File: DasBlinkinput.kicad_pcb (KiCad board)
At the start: 4 copper layers, 25.4 x 50.8 mm, 34 parts, among them P101 CONN_01X02, P102 CONN_01X01, P103 CONN_01X01, P104 CONN_01X01, P105 CONN_01X05, P201 CONN_01X01, P301 CONN_01X01, P401 CONN_01X01, P501 CONN_01X01, U101 LP2980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

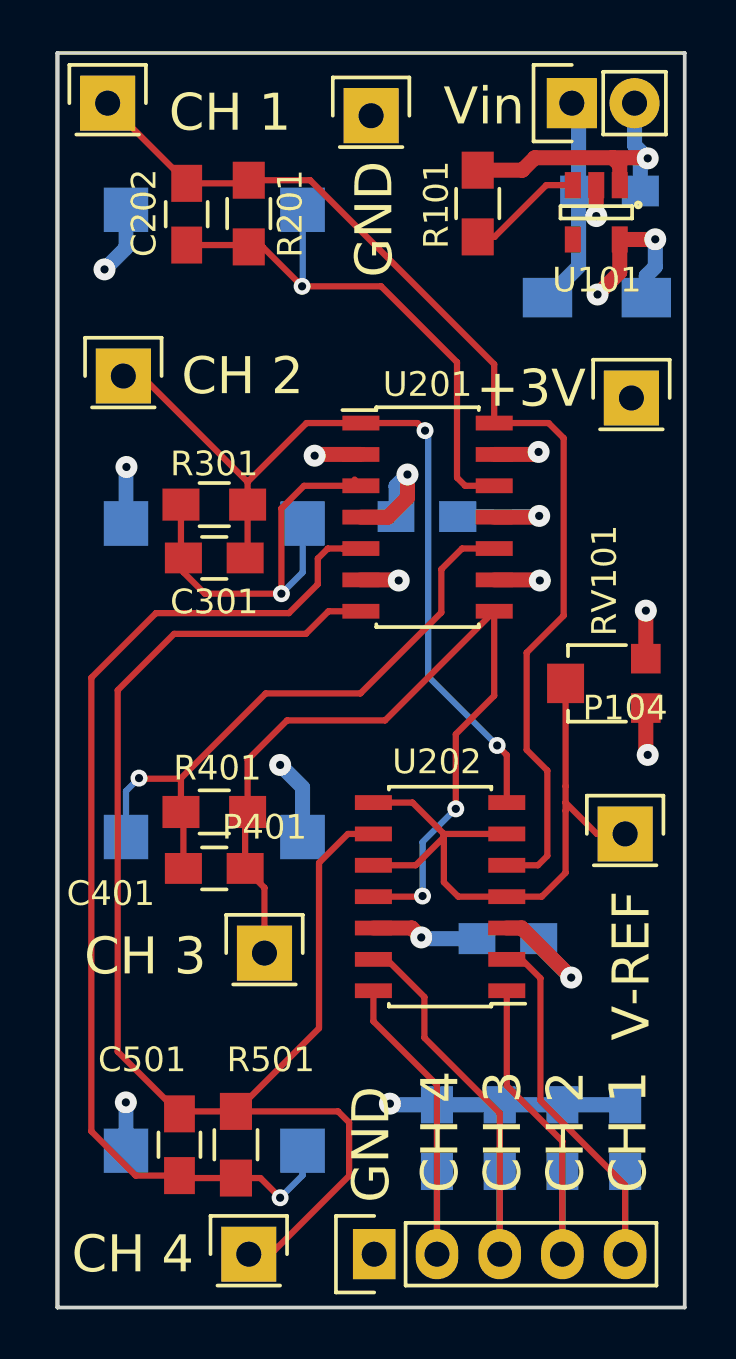
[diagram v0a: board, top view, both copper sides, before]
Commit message: resized labels and added board name and rev
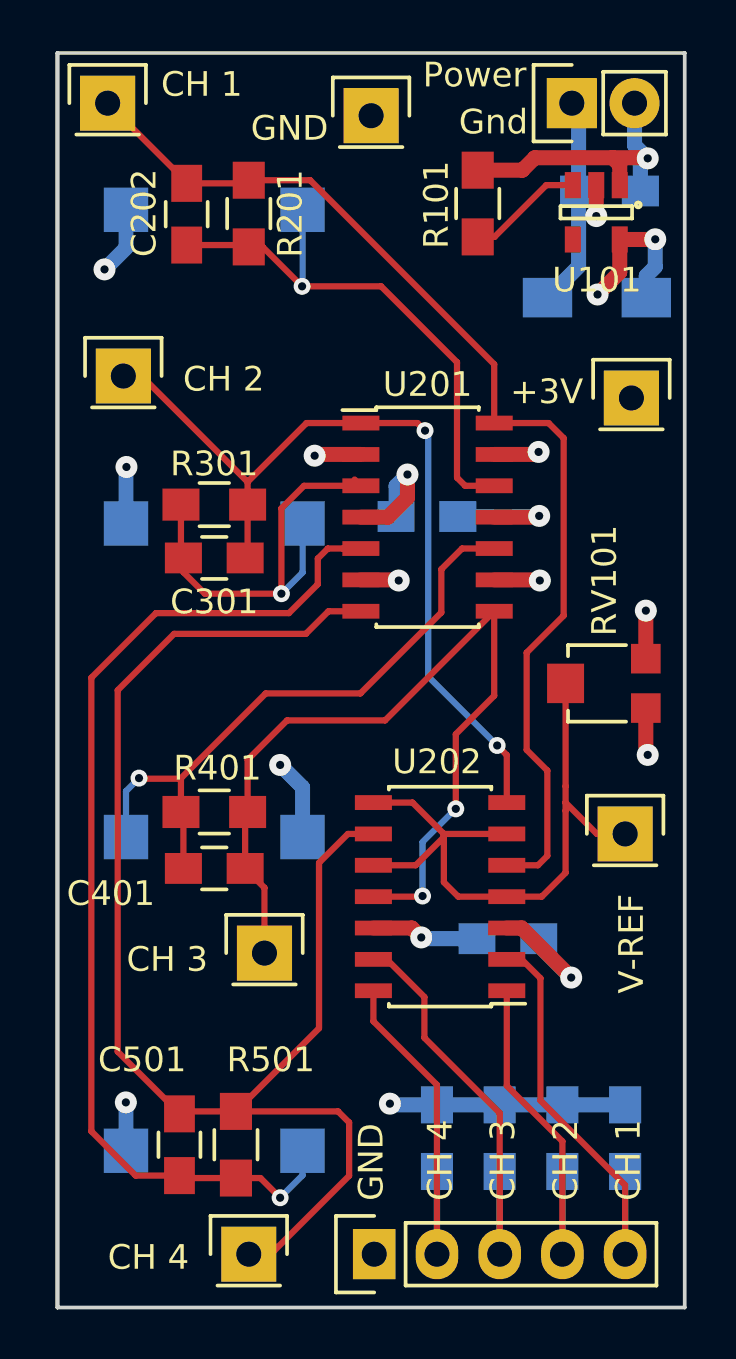
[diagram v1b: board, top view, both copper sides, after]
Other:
- board text added: "DasBlinkInput Rev. 0"
- board text added: "Gnd"
- board text added: "Power"
- board text removed: "Vin"
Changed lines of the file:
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@@
     (links 74)
     (no_connects 0)
-    (area 130.480999 65.710999 156.031001 116.661001)
+    (area 127.425667 61.539 158.959334 119.589333)
     (thickness 1.6)
-    (drawings 19)
+    (drawings 21)
     (tracks 259)
     (zones 0)
@@
   (layers
     (0 F.Cu signal)
-    (1 PWR.Cu signal)
-    (2 GND.Cu signal)
+    (1 PWR.Cu signal hide)
+    (2 GND.Cu signal hide)
     (31 B.Cu signal)
     (32 B.Adhes user)
@@
     (35 F.Paste user)
     (36 B.SilkS user)
-    (37 F.SilkS user)
+    (37 F.SilkS user hide)
     (38 B.Mask user)
     (39 F.Mask user)
@@
     (tags "capacitor 0805")
     (attr smd)
-    (fp_text reference C201 (at 0 2.1) (layer B.SilkS)
+    (fp_text reference C201 (at 1.5494 2.0574) (layer B.SilkS)
       (effects (font (size 1 1) (thickness 0.15)) (justify mirror))
     )
@@
   (module DasBlinkinput:VBPW34S (layer B.Cu)
     (at 136.906 97.536)
-    (fp_text reference PD401 (at 0 -3) (layer B.SilkS)
+    (fp_text reference PD401 (at -0.381 -3.302) (layer B.SilkS)
       (effects (font (size 1 1) (thickness 0.15)) (justify mirror))
     )
@@
   (module DasBlinkinput:VBPW34S (layer B.Cu)
     (at 136.906 110.236 180)
-    (fp_text reference PD501 (at 0 -3 180) (layer B.SilkS)
+    (fp_text reference PD501 (at 0.127 3.048 180) (layer B.SilkS)
       (effects (font (size 1 1) (thickness 0.15)) (justify mirror))
     )
@@
     (descr "Through hole pin header")
     (tags "pin header")
-    (fp_text reference P401 (at 0 -5.1) (layer F.SilkS)
+    (fp_text reference P401 (at 0 -5.1) (layer F.SilkS) hide
       (effects (font (size 1 1) (thickness 0.15)))
     )
@@
     (descr "Through hole pin header")
     (tags "pin header")
-    (fp_text reference P104 (at 0 -5.1) (layer F.SilkS)
+    (fp_text reference P104 (at 0 -5.1) (layer F.SilkS) hide
       (effects (font (size 1 1) (thickness 0.15)))
     )
@@
     )
   )
-  (gr_text V-REF (at 153.797 102.743 90) (layer F.SilkS)
-    (effects (font (size 1.5 1.5) (thickness 0.3)))
-  )
-  (gr_text GND (at 143.383 72.517 90) (layer F.SilkS)
-    (effects (font (size 1.5 1.5) (thickness 0.3)))
-  )
-  (gr_text +3V (at 149.733 79.375) (layer F.SilkS)
-    (effects (font (size 1.5 1.5) (thickness 0.3)))
-  )
-  (gr_text Vin (at 147.828 67.945) (layer F.SilkS)
-    (effects (font (size 1.5 1.5) (thickness 0.3)))
-  )
-  (gr_text "Input Voltage:\n+3.2V to +16V" (at 140.843 78.232) (layer B.SilkS)
-    (effects (font (size 1.5 1.5) (thickness 0.3)) (justify mirror))
-  )
-  (gr_text "CH 4" (at 133.604 114.427) (layer F.SilkS)
-    (effects (font (size 1.5 1.5) (thickness 0.3)))
-  )
-  (gr_text "CH 3" (at 134.112 102.362) (layer F.SilkS)
-    (effects (font (size 1.5 1.5) (thickness 0.3)))
-  )
-  (gr_text "CH 2" (at 138.049 78.867) (layer F.SilkS)
-    (effects (font (size 1.5 1.5) (thickness 0.3)))
-  )
-  (gr_text "CH 1" (at 137.541 68.199) (layer F.SilkS)
-    (effects (font (size 1.5 1.5) (thickness 0.3)))
-  )
-  (gr_text "CH 4" (at 146.05 109.474 90) (layer F.SilkS)
-    (effects (font (size 1.5 1.5) (thickness 0.3)))
-  )
-  (gr_text "CH 3" (at 148.59 109.474 90) (layer F.SilkS)
-    (effects (font (size 1.5 1.5) (thickness 0.3)))
-  )
-  (gr_text "CH 2" (at 151.13 109.474 90) (layer F.SilkS)
-    (effects (font (size 1.5 1.5) (thickness 0.3)))
-  )
-  (gr_text "CH 1" (at 153.67 109.474 90) (layer F.SilkS)
-    (effects (font (size 1.5 1.5) (thickness 0.3)))
-  )
-  (gr_text GND (at 143.256 109.982 90) (layer F.SilkS)
-    (effects (font (size 1.5 1.5) (thickness 0.3)))
+  (gr_text "DasBlinkInput\nRev. 0" (at 149.225 90.932) (layer B.SilkS)
+    (effects (font (size 1 1) (thickness 0.15)) (justify left mirror))
+  )
+  (gr_text Gnd (at 148.209 68.58) (layer F.SilkS)
+    (effects (font (size 1 1) (thickness 0.15)))
+  )
+  (gr_text V-REF (at 153.797 101.854 90) (layer F.SilkS)
+    (effects (font (size 1 1) (thickness 0.15)))
+  )
+  (gr_text GND (at 139.954 68.834) (layer F.SilkS)
+    (effects (font (size 1 1) (thickness 0.15)))
+  )
+  (gr_text +3V (at 150.368 79.502) (layer F.SilkS)
+    (effects (font (size 1 1) (thickness 0.15)))
+  )
+  (gr_text Power (at 147.447 66.675) (layer F.SilkS)
+    (effects (font (size 1 1) (thickness 0.15)))
+  )
+  (gr_text "Input Voltage:\n+3.2V to +16V" (at 142.748 77.978) (layer B.SilkS)
+    (effects (font (size 1 1) (thickness 0.15)) (justify mirror))
+  )
+  (gr_text "CH 4" (at 134.239 114.554) (layer F.SilkS)
+    (effects (font (size 1 1) (thickness 0.15)))
+  )
+  (gr_text "CH 3" (at 135.001 102.489) (layer F.SilkS)
+    (effects (font (size 1 1) (thickness 0.15)))
+  )
+  (gr_text "CH 2" (at 137.287 78.994) (layer F.SilkS)
+    (effects (font (size 1 1) (thickness 0.15)))
+  )
+  (gr_text "CH 1" (at 136.398 67.056) (layer F.SilkS)
+    (effects (font (size 1 1) (thickness 0.15)))
+  )
+  (gr_text "CH 4" (at 146.05 112.268 90) (layer F.SilkS)
+    (effects (font (size 1 1) (thickness 0.15)) (justify left))
+  )
+  (gr_text "CH 3" (at 148.59 112.268 90) (layer F.SilkS)
+    (effects (font (size 1 1) (thickness 0.15)) (justify left))
+  )
+  (gr_text "CH 2" (at 151.13 112.268 90) (layer F.SilkS)
+    (effects (font (size 1 1) (thickness 0.15)) (justify left))
+  )
+  (gr_text "CH 1" (at 153.67 112.268 90) (layer F.SilkS)
+    (effects (font (size 1 1) (thickness 0.15)) (justify left))
+  )
+  (gr_text GND (at 143.256 112.268 90) (layer F.SilkS)
+    (effects (font (size 1 1) (thickness 0.15)) (justify left))
   )
   (gr_line (start 130.556 116.586) (end 155.956 116.586) (angle 90) (layer Edge.Cuts) (width 0.15))
